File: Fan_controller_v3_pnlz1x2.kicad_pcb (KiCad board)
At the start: 4 copper layers, 50 x 50 mm, 104 parts, among them J1 Load2, J2 Dig_mod_iface, K1 HFD2_005-S-L2-D_Split, K2 HFD2_005-S-L2-D_Split, Q1 2N5551S, Q2 2N5551S, Q3 BSS138, Q4 BSS138, Q5 2N5551S, Q6 2N5551S, U1 ADuM1251ARZ, U2 PCA9536DP

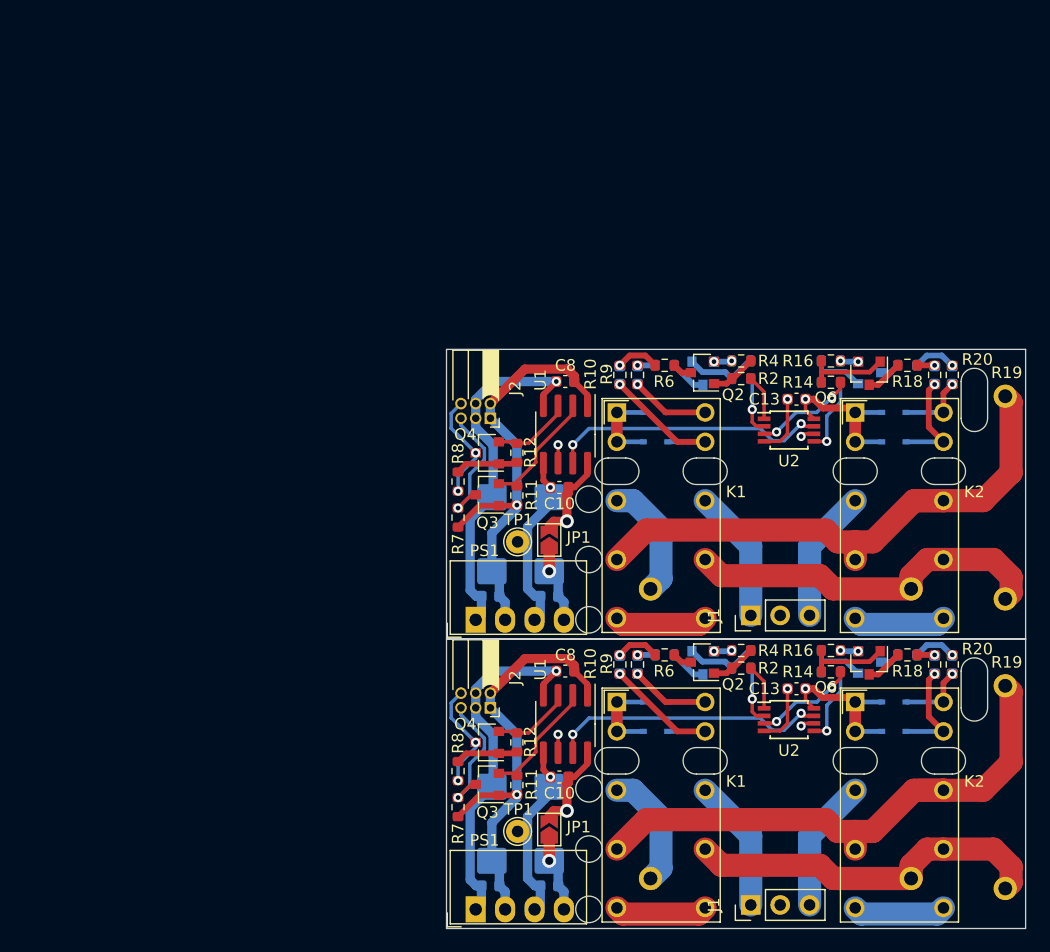
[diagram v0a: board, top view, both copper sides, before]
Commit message: Сформирован перечень элементов, 3D-модель, исправлены ошибки, реализована панелизация платы.
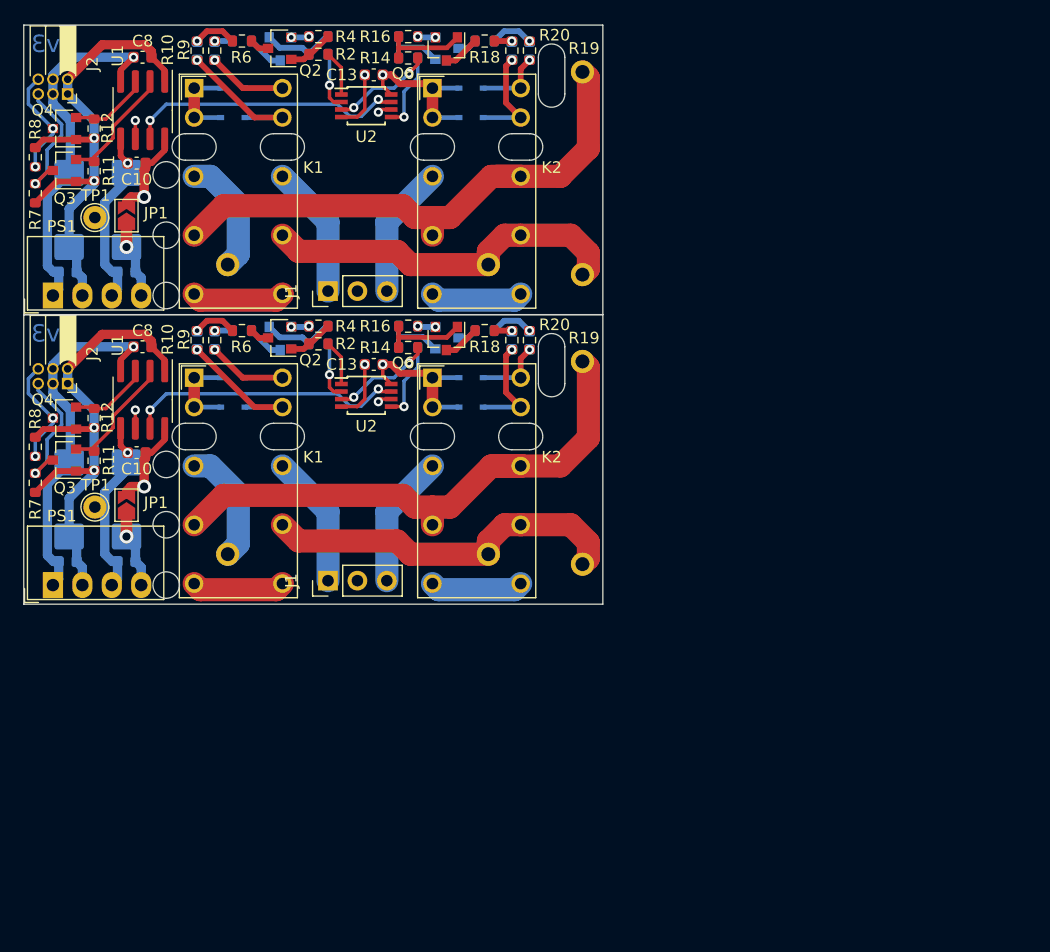
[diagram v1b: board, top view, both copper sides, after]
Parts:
- moved C7 46.0 mm to (92.7, 67.5)
- moved C7 46.0 mm to (92.7, 42.5)
- moved C1 46.0 mm to (48.4, 79.5)
- moved C1 46.0 mm to (48.4, 54.5)
- moved C13 46.0 mm to (74.7, 42.8)
- moved D1 46.0 mm to (62.5, 68.9)
- moved D2 46.0 mm to (62.5, 71.5)
- moved D2 46.0 mm to (62.5, 46.5)
- moved PS1 46.0 mm to (47.0, 61.8)
- moved Q1 46.0 mm to (66.6, 40.6)
- moved Q6 46.0 mm to (81.0, 40.6)
- moved R11 46.0 mm to (50.6, 51.1)
- moved R7 46.0 mm to (45.5, 53.0)
- moved R8 46.0 mm to (45.5, 49.9)
- moved D1 46.0 mm to (62.5, 43.9)
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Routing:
- net +5P: vias 2 -> 4
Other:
- board text added: "v3"
